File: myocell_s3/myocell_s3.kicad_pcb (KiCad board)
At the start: 4 copper layers, 51 x 68 mm, 102 parts, among them J1 Conn_01x08, J2 IN3P, J3 IN3N, J4 IN4P, J5 Battery Connector JC2, J6 IN4N, J7 USB_C_Receptacle_USB2.0_16P, J8 RLD, Q3 DMG3404L, SW1 SW_Push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

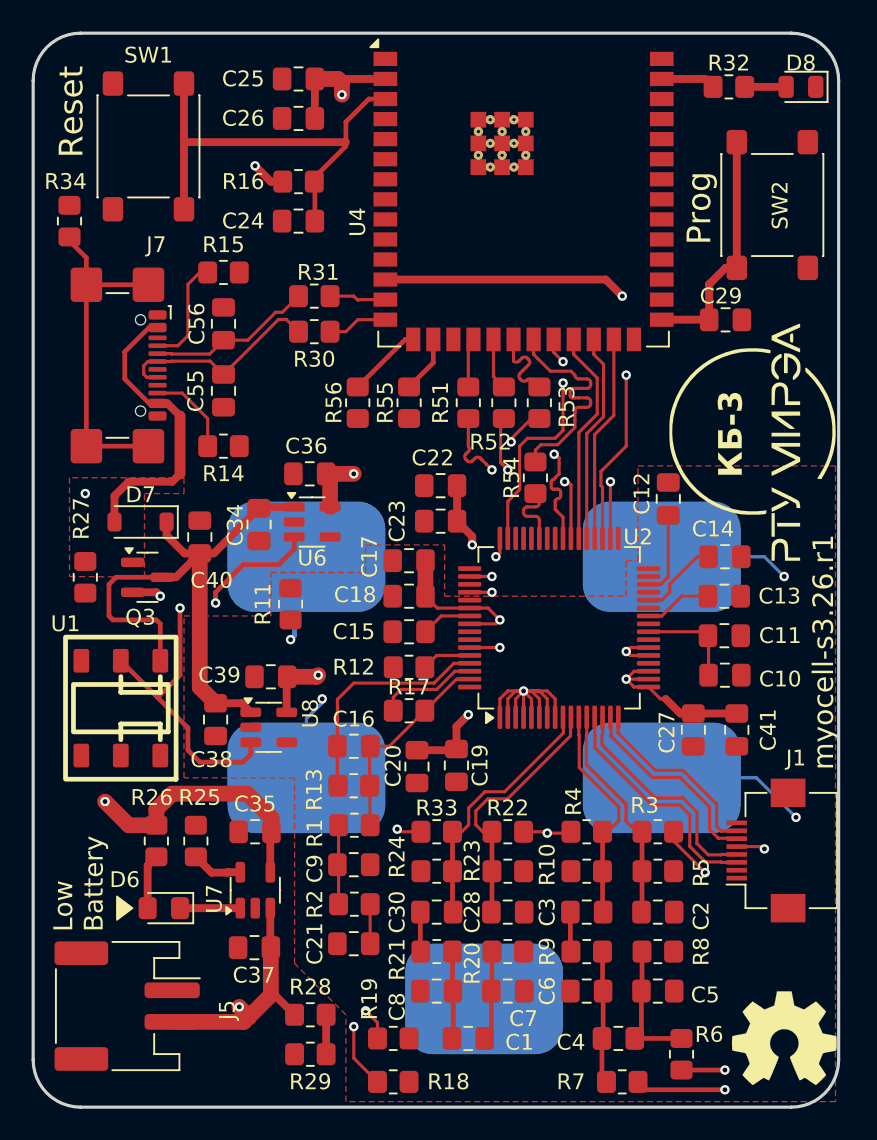
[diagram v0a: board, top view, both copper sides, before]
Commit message: placing polygons
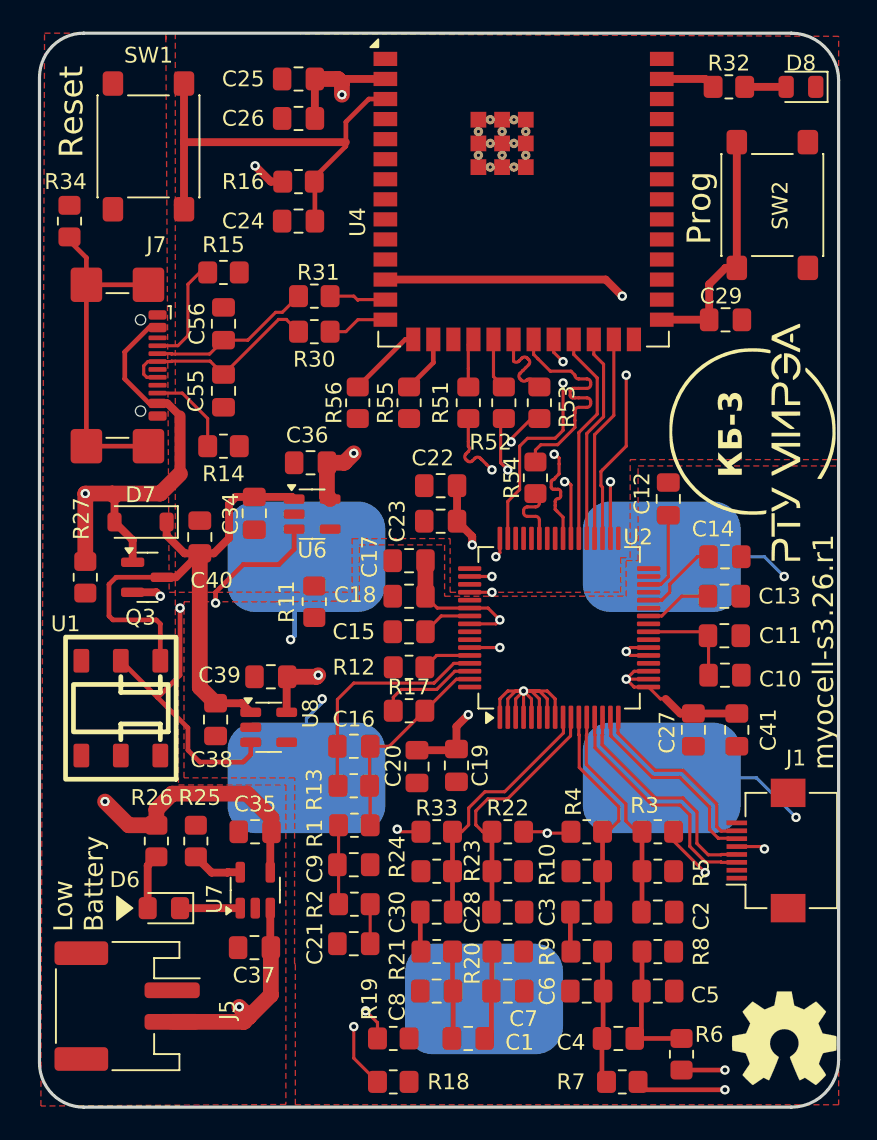
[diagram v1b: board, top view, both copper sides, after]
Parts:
- removed R28, R29: 10k, Resistor_SMD:R_0805_2012Metric_Pad1.20x1.40mm_HandSolder
- moved R11 1.51 mm to (171.0, 85.6)
- moved C34 0.77 mm to (167.2, 80.0)
- moved C36 0.70 mm to (170.8, 76.8)
- moved U6 0.50 mm to (170.9, 80.0)
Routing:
- net /power_supply/VUSB/2.1A: track 55.6 -> 65.0 mm
- net /cpu_wroom_esp32/bat_mon: track 2.50 -> 0.00 mm
- net /power_supply/BAT: track 20.2 -> 18.5 mm
- net VIN: track 37.3 -> 38.9 mm
- net PWR_ENA: track 28.9 -> 29.4 mm
- added copper zone on F.Cu, net GND
- removed copper zone on F.Cu, net /power_supply/VUSB/2.1A
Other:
- board size 51 x 68 mm -> 50.6 x 68 mm

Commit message: polygon tuning
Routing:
- net /adc_8/RLD: track 2.50 -> 34.6 mm, vias 0 -> 2
- net Net-(C1-Pad1): track 5.69 -> 12.2 mm
- net Net-(C1-Pad2): track 5.55 -> 8.26 mm
- net Net-(C28-Pad1): track 0.00 -> 2.52 mm
- net GND: track 0.00 -> 2.45 mm
- added copper zone on B.Cu, net GND
- added copper zone on In1.Cu, net GND
- added copper zone on In1.Cu, net GNDA
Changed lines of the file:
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@@
 		(tags "resistor handsolder")
 		(property "Reference" "R19"
-			(at -1.5 -2.5 90)
+			(at -2.6 -0.05 90)
 			(layer "F.SilkS")
 			(effects
@@
 		(tags "resistor handsolder")
 		(property "Reference" "R14"
-			(at 0 -1.75 180)
+			(at -3.35 1.15 180)
 			(layer "F.SilkS")
 			(effects
@@
 		(tags "capacitor handsolder")
 		(property "Reference" "C8"
-			(at -2.5 1 90)
+			(at -2.75 0.35 180)
 			(layer "F.SilkS")
 			(effects
@@
 		(tags "resistor handsolder")
 		(property "Reference" "R4"
-			(at -0.8375 -1.9125 90)
+			(at 0.15 -1.7625 180)
 			(layer "F.SilkS")
 			(effects
@@
 		(tags "resistor handsolder")
 		(property "Reference" "R8"
-			(at 2.75 0 90)
+			(at 2.75 0 180)
 			(layer "F.SilkS")
 			(effects
@@
 		(tags "connector JST PH horizontal")
 		(property "Reference" "J5"
-			(at 0.25 -6.35 90)
+			(at 3.8 -5.65 180)
 			(layer "F.SilkS")
 			(effects
@@
 		(tags "capacitor handsolder")
 		(property "Reference" "C7"
-			(at 1 1.75 180)
+			(at 0.15 1.55 180)
 			(layer "F.SilkS")
 			(effects
@@
 		(tags "resistor handsolder")
 		(property "Reference" "R5"
-			(at -2.75 -0.0875 90)
+			(at -2.75 -0.0875 180)
 			(layer "F.SilkS")
 			(effects
@@
 		(tags "capacitor handsolder")
 		(property "Reference" "C36"
-			(at -0.2125 -1.75 0)
+			(at 3.6375 0 0)
 			(layer "F.SilkS")
 			(effects
@@
 		(tags "capacitor handsolder")
 		(property "Reference" "C2"
-			(at -2.75 -0.25 90)
+			(at -2.75 -0.25 180)
 			(layer "F.SilkS")
 			(effects
@@
 		(tags "capacitor handsolder")
 		(property "Reference" "C1"
-			(at -3.25 -0.25 0)
+			(at 0.15 1.45 0)
 			(layer "F.SilkS")
 			(effects
@@
 	)
 	(segment
+		(start 196.2 108.8)
+		(end 196.2 103.8)
+		(width 0.2)
+		(layer "F.Cu")
+		(net 11)
+	)
+	(segment
+		(start 174.5375 107.25)
+		(end 174.5375 109.5375)
+		(width 0.2)
+		(layer "F.Cu")
+		(net 11)
+	)
+	(segment
+		(start 196.9 103.1)
+		(end 197.75 103.1)
+		(width 0.2)
+		(layer "F.Cu")
+		(net 11)
+	)
+	(segment
+		(start 174.5375 109.5375)
+		(end 175.2 110.2)
+		(width 0.2)
+		(layer "F.Cu")
+		(net 11)
+	)
+	(segment
+		(start 195.6 109.4)
+		(end 196.2 108.8)
+		(width 0.2)
+		(layer "F.Cu")
+		(net 11)
+	)
+	(segment
+		(start 196.2 103.8)
+		(end 196.9 103.1)
+		(width 0.2)
+		(layer "F.Cu")
+		(net 11)
+	)
+	(via
+		(at 175.2 110.2)
+		(size 0.6)
+		(drill 0.3)
+		(layers "F.Cu" "B.Cu")
+		(net 11)
+	)
+	(via
+		(at 195.6 109.4)
+		(size 0.6)
+		(drill 0.3)
+		(layers "F.Cu" "B.Cu")
+		(net 11)
+	)
+	(segment
+		(start 194.25 110.75)
+		(end 195.6 109.4)
+		(width 0.2)
+		(layer "B.Cu")
+		(net 11)
+	)
+	(segment
+		(start 175.75 110.75)
+		(end 181.75 110.75)
+		(width 0.2)
+		(layer "B.Cu")
+		(net 11)
+	)
+	(segment
+		(start 181.75 110.75)
+		(end 194.25 110.75)
+		(width 0.2)
+		(layer "B.Cu")
+		(net 11)
+	)
+	(segment
+		(start 175.2 110.2)
+		(end 175.75 110.75)
+		(width 0.2)
+		(layer "B.Cu")
+		(net 11)
+	)
+	(segment
 		(start 171.8 76.8)
 		(end 171.8 78.9)
@@
 	)
 	(segment
+		(start 165.3 93.55)
+		(end 164.75 94.1)
+		(width 0.5)
+		(layer "F.Cu")
+		(net 13)
+	)
+	(segment
+		(start 166.975 93.55)
+		(end 165.3 93.55)
+		(width 0.5)
+		(layer "F.Cu")
+		(net 13)
+	)
+	(segment
 		(start 162.75 56.5)
 		(end 162.75 60.75)
@@
 	)
 	(segment
+		(start 179.7125 113.25)
+		(end 177 113.25)
+		(width 0.2)
+		(layer "F.Cu")
+		(net 19)
+	)
+	(segment
 		(start 179.7875 113.175)
 		(end 179.7125 113.25)
@@
 	)
 	(segment
+		(start 181.7875 113.25)
+		(end 181.7875 114.2125)
+		(width 0.2)
+		(layer "F.Cu")
+		(net 20)
+	)
+	(segment
+		(start 181.7875 114.2125)
+		(end 180 116)
+		(width 0.2)
+		(layer "F.Cu")
+		(net 20)
+	)
+	(segment
 		(start 182.2125 110.25)
 		(end 182.2125 112.825)
@@
 	)
 	(segment
+		(start 180 116)
+		(end 177 116)
+		(width 0.2)
+		(layer "F.Cu")
+		(net 20)
+	)
+	(segment
 		(start 187.2125 105.25)
 		(end 187.2125 107.7125)
@@
 	)
 	(segment
+		(start 184.2875 105.25)
+		(end 184.2875 107.7125)
+		(width 0.2)
+		(layer "F.Cu")
+		(net 31)
+	)
+	(segment
+		(start 184.2875 107.7125)
+		(end 184.25 107.75)
+		(width 0.2)
+		(layer "F.Cu")
+		(net 31)
+	)
+	(segment
 		(start 177.7125 107.7125)
 		(end 177.75 107.75)
@@
 		(net 1)
 		(net_name "GNDA")
-		(layer "F.Cu")
+		(layers "F.Cu" "In1.Cu")
 		(hatch edge 0.5)
 		(priority 8)
@@
 			(thermal_gap 0.5)
 			(thermal_bridge_width 0.5)
+			(island_removal_mode 1)
+			(island_area_min 10)
 		)
 		(polygon
 			(pts
 				(xy 173.85 82) (xy 179.25 82) (xy 179.25 85.25) (xy 190.75 85.25) (xy 190.75 83) (xy 191.5 83) (xy 191.5 77)
-				(xy 204.2 77) (xy 204.2 117.45) (xy 169.8 117.45) (xy 169.8 108.55) (xy 169.75 108.5) (xy 169.75 96.75)
-				(xy 162.75 96.75) (xy 162.75 85.6) (xy 168.4 85.6) (xy 168.4 85.6) (xy 173.85 85.554583)
+				(xy 204.2 77) (xy 204.2 117.65) (xy 169.8 117.65) (xy 169.8 96.95) (xy 162.549103 96.95) (xy 162.599996 85.600822)
+				(xy 173.85 85.554583)
 			)
 		)
@@
 		(net 13)
 		(net_name "GND")
-		(layer "F.Cu")
+		(layers "F.Cu" "In1.Cu")
 		(hatch edge 0.5)
 		(connect_pads
@@
 			(thermal_gap 0.5)
 			(thermal_bridge_width 0.5)
+			(island_removal_mode 1)
+			(island_area_min 10)
 		)
 		(polygon
 			(pts
-				(xy 161.6 49.8) (xy 161.810779 85) (xy 173.4 85) (xy 173.4 81.6) (xy 179.6 81.6) (xy 179.6 85) (xy 190.4 85)
-				(xy 190.4 82.8) (xy 191 82.8) (xy 191 76.6) (xy 204.2 76.6) (xy 204.2 49.8) (xy 161.6 49.6) (xy 161.6 50)
+				(xy 160.8 49.594312) (xy 160.8 85) (xy 173.4 85) (xy 173.4 81.6) (xy 179.6 81.6) (xy 179.6 84.8)
+				(xy 190.2 84.8) (xy 190.2 82.6) (xy 191 82.6) (xy 191 76.6) (xy 204.2 76.6) (xy 204.2 49.8)
 			)
 		)
@@
 		(net 13)
 		(net_name "GND")
-		(layer "F.Cu")
+		(layers "F.Cu" "In1.Cu")
 		(hatch edge 0.5)
 		(priority 9)
@@
 		(polygon
 			(pts
-				(xy 153.920224 49.6) (xy 162.2 49.6) (xy 162.2 90.6) (xy 162.4 90.6) (xy 162.4 97.2) (xy 169.2 97.2)
-				(xy 169.2 117.430216) (xy 153.68953 117.527844)
+				(xy 153.582646 49.6) (xy 161.982646 49.6) (xy 161.982646 97.6) (xy 169.382646 97.6) (xy 169.382646 117.6)
+				(xy 153.582646 117.6)
+			)
+		)
+	)
+	(zone
+		(net 13)
+		(net_name "GND")
+		(layer "B.Cu")
+		(hatch edge 0.5)
+		(connect_pads
+			(clearance 0.2)
+		)
+		(min_thickness 0.2)
+		(filled_areas_thickness no)
+		(fill yes
+			(thermal_gap 0.5)
+			(thermal_bridge_width 0.5)
+			(island_removal_mode 1)
+			(island_area_min 10)
+		)
+		(polygon
+			(pts
+				(xy 153.6 49.6) (xy 204.2 49.6) (xy 204.2 117.6) (xy 153.6 117.6)
 			)
 		)

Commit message: start DRC
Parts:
- moved REF** 0.86 mm to (200.6, 112.4)
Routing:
- net /usb_d-: track 10.5 -> 15.8 mm, vias 0 -> 2
- net Net-(C2-Pad1): track 0.00 -> 2.52 mm
- net +3.3V: track 62.7 -> 65.0 mm, vias 7 -> 6
- net PWR_ENA: track 29.4 -> 27.1 mm
- net GND: track 2.45 -> 1.56 mm, vias 0 -> 3

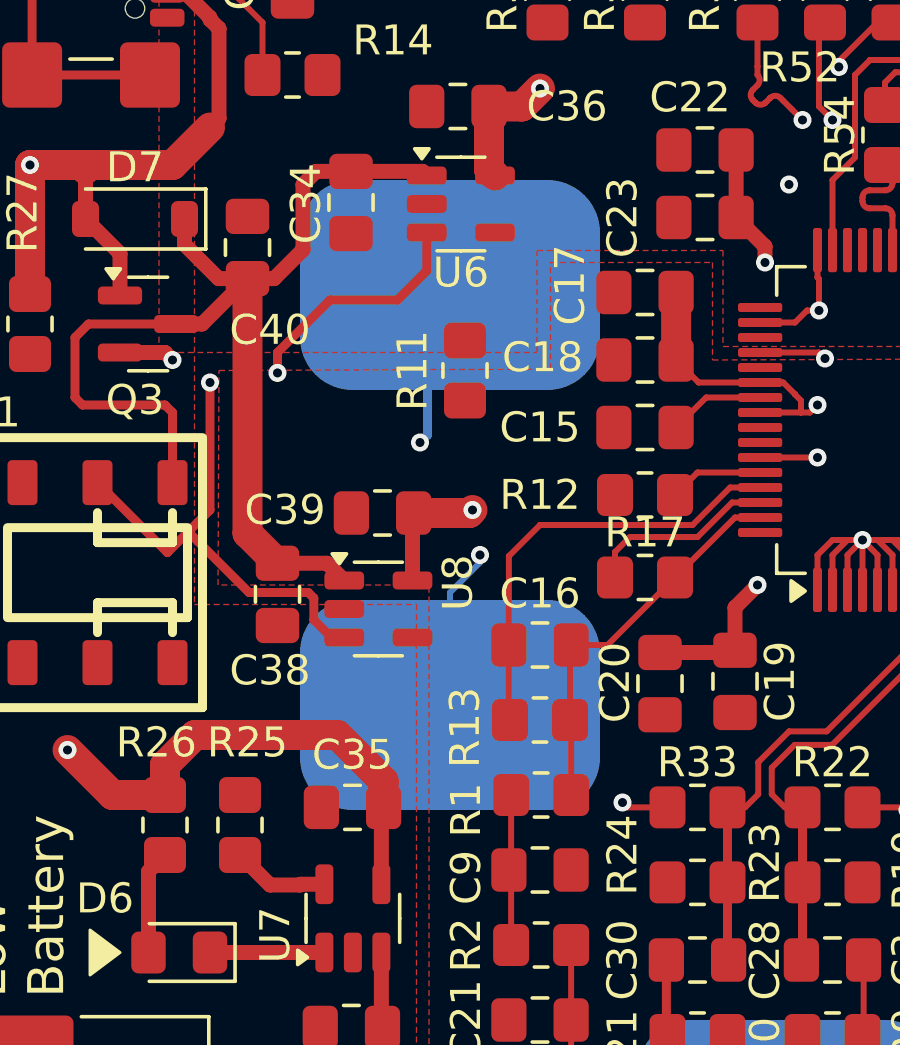
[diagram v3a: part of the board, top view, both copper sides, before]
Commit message: adjust electrode positions
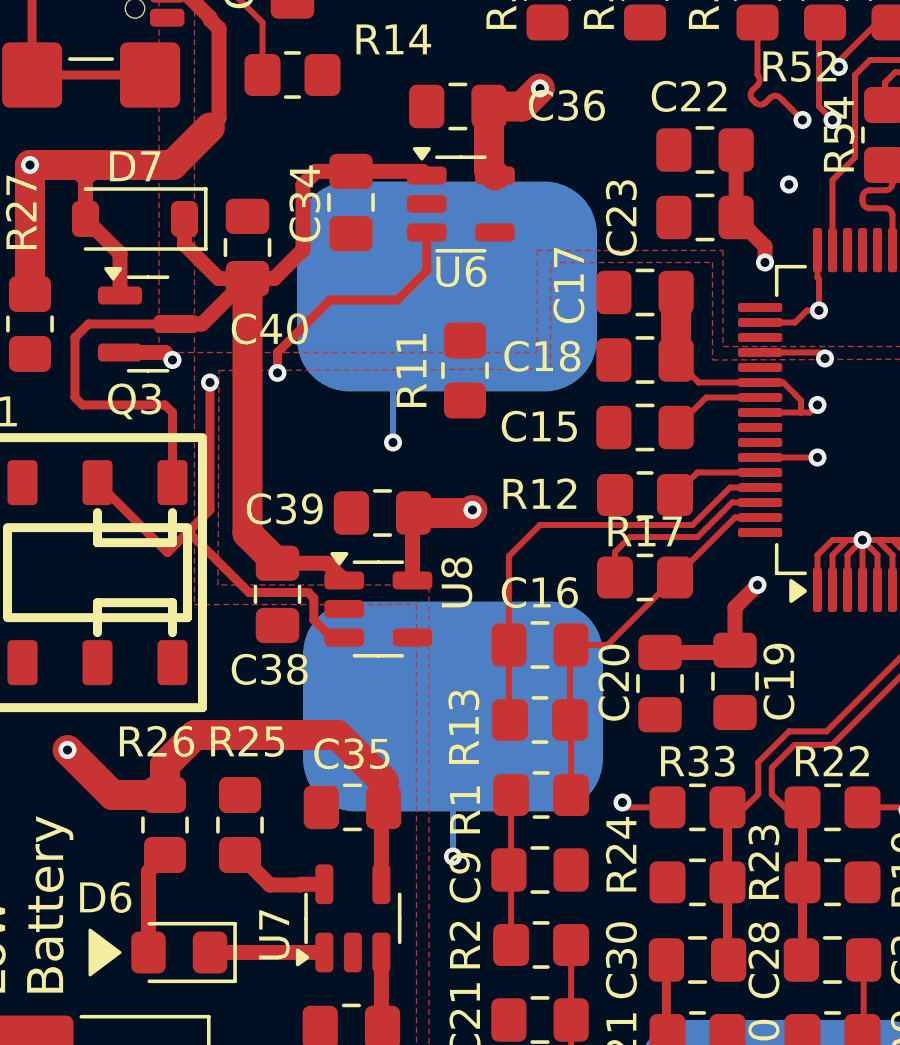
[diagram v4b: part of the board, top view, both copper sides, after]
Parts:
- moved J4 14.1 mm to (170.6, 96.8)
- moved J6 14.0 mm to (170.4, 82.8)
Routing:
- net /adc_8/in4f+: track 35.4 -> 21.0 mm
- net /adc_8/in4f-: track 28.9 -> 34.1 mm
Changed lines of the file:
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@@
 	(footprint "emg:EMG_PAD_10_7"
 		(layer "B.Cu")
-		(at 170.5 82.75 180)
+		(at 170.6 96.8 180)
 		(property "Reference" "J4"
 			(at -6.25 6 0)
@@
 	(footprint "emg:EMG_PAD_10_7"
 		(layer "B.Cu")
-		(at 170.5 96.75 180)
+		(at 170.4 82.8 180)
 		(property "Reference" "J6"
 			(at -6.75 6 0)
@@
 		)
 	)
+	(dimension
+		(type orthogonal)
+		(layer "Dwgs.User")
+		(pts
+			(xy 204.2 117.65) (xy 204.2 49.8)
+		)
+		(height 5.6)
+		(orientation 1)
+		(format
+			(prefix "")
+			(suffix "")
+			(units 3)
+			(units_format 1)
+			(precision 4)
+		)
+		(style
+			(thickness 0.1)
+			(arrow_length 1.27)
+			(text_position_mode 0)
+			(arrow_direction outward)
+			(extension_height 0.58642)
+			(extension_offset 0.5)
+			(keep_text_aligned yes)
+		)
+		(gr_text "67.8500 mm"
+			(at 208.65 83.725 90)
+			(layer "Dwgs.User")
+			(effects
+				(font
+					(size 1 1)
+					(thickness 0.15)
+				)
+			)
+		)
+	)
+	(dimension
+		(type orthogonal)
+		(layer "Dwgs.User")
+		(pts
+			(xy 153.6 117.6) (xy 204.2 117.6)
+		)
+		(height 6.2)
+		(orientation 0)
+		(format
+			(prefix "")
+			(suffix "")
+			(units 3)
+			(units_format 1)
+			(precision 4)
+		)
+		(style
+			(thickness 0.1)
+			(arrow_length 1.27)
+			(text_position_mode 0)
+			(arrow_direction outward)
+			(extension_height 0.58642)
+			(extension_offset 0.5)
+			(keep_text_aligned yes)
+		)
+		(gr_text "50.6000 mm"
+			(at 178.9 122.65 0)
+			(layer "Dwgs.User")
+			(effects
+				(font
+					(size 1 1)
+					(thickness 0.15)
+				)
+			)
+		)
+	)
 	(segment
 		(start 172.4625 102.7125)
@@
 	)
 	(via
-		(at 169.5 88)
+		(at 170.6 101.8)
 		(size 0.6)
 		(drill 0.3)
@@
 	)
 	(segment
-		(start 169.75 83)
-		(end 169.75 87.75)
-		(width 0.3)
-		(layer "B.Cu")
-		(net 93)
-	)
-	(segment
-		(start 169.75 87.75)
-		(end 169.5 88)
-		(width 0.3)
-		(layer "B.Cu")
-		(net 93)
-	)
-	(segment
-		(start 169.5 90.725)
-		(end 169.5 88)
+		(start 170.6 101.8)
+		(end 170.6 96.8)
 		(width 0.2)
-		(layer "In2.Cu")
+		(layer "B.Cu")
 		(net 93)
 	)
 	(segment
-		(start 170.775 92)
-		(end 169.5 90.725)
+		(start 170.775 109.093199)
+		(end 170.775 101.975)
 		(width 0.2)
 		(layer "In2.Cu")
@@
 	)
 	(segment
-		(start 173.5 111.818199)
-		(end 170.775 109.093199)
+		(start 173.5 112.5)
+		(end 173.5 111.818199)
 		(width 0.2)
 		(layer "In2.Cu")
@@
 	)
 	(segment
-		(start 170.775 109.093199)
-		(end 170.775 92)
+		(start 170.775 101.975)
+		(end 170.6 101.8)
 		(width 0.2)
 		(layer "In2.Cu")
@@
 	)
 	(segment
-		(start 173.5 112.5)
-		(end 173.5 111.818199)
+		(start 173.5 111.818199)
+		(end 170.775 109.093199)
 		(width 0.2)
 		(layer "In2.Cu")
@@
 	)
 	(via
-		(at 171.5 91.75)
+		(at 168.6 88)
 		(size 0.6)
 		(drill 0.3)
@@
 	)
 	(segment
-		(start 171.5 91.75)
-		(end 171.5 92)
+		(start 168.6 88)
+		(end 168.6 84.6)
 		(width 0.2)
 		(layer "B.Cu")
@@
 	)
 	(segment
-		(start 171.5 92)
-		(end 170.5 93)
+		(start 168.6 84.6)
+		(end 170.4 82.8)
 		(width 0.2)
 		(layer "B.Cu")
@@
 	)
 	(segment
-		(start 170.5 93)
-		(end 170.5 96.75)
+		(start 168.6 90.681802)
+		(end 168.6 88)
 		(width 0.2)
-		(layer "B.Cu")
+		(layer "In2.Cu")
 		(net 94)
 	)
 	(segment
-		(start 171.225 92)
-		(end 171.25 92)
+		(start 171.225 108.906801)
+		(end 171.225 93.306802)
 		(width 0.2)
 		(layer "In2.Cu")
@@
 	)
 	(segment
-		(start 171.25 92)
-		(end 171.5 91.75)
+		(start 171.225 93.306802)
+		(end 168.759099 90.840901)
 		(width 0.2)
 		(layer "In2.Cu")
@@
 	)
 	(segment
-		(start 171.225 108.906801)
-		(end 171.225 92)
+		(start 168.759099 90.840901)
+		(end 168.6 90.681802)
 		(width 0.2)
 		(layer "In2.Cu")
@@
 			(pts
 				(xy 160.8 49.594312) (xy 160.8 85) (xy 173.4 85) (xy 173.4 81.6) (xy 179.6 81.6) (xy 179.6 84.8)
-				(xy 191 84.8) (xy 191 82.6) (xy 191 82.6) (xy 191 76.6) (xy 204.2 76.6) (xy 204.2 49.8)
+				(xy 191 84.8) (xy 191 82.6) (xy 191 76.6) (xy 204.2 76.6) (xy 204.2 49.8)
 			)
 		)

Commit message: DRC
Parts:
- added R28: 10k, Resistor_SMD:R_0805_2012Metric_Pad1.20x1.40mm_HandSolder, F.Cu at (156.2, 84.8)
- added R29: 10k, Resistor_SMD:R_0805_2012Metric_Pad1.20x1.40mm_HandSolder, F.Cu at (170.0, 63.6)
- moved R27 3.86 mm to (156.2, 80.2)
- moved R30 1.35 mm to (170.0, 69.4)
- moved R31 1.25 mm to (170.0, 67.0)
- moved R16 0.80 mm to (170.0, 58.2)
- moved C24 0.70 mm to (170.0, 60.8)
- moved R14 0.29 mm to (165.4, 76.0)
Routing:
- net /cpu_wroom_esp32/bat_mon: track 0.00 -> 45.5 mm, vias 0 -> 2
- net VIN: track 38.9 -> 32.3 mm
- net /power_supply/BAT: track 18.5 -> 22.1 mm
- net PWR_ENA: track 27.1 -> 30.6 mm
- net /power_supply/VUSB/2.1A: track 65.2 -> 62.3 mm
- net GND: track 1.56 -> 4.02 mm, vias 3 -> 11
- net /usb_d+: track 13.5 -> 11.5 mm
- net /cpu_wroom_esp32/D-: track 3.62 -> 5.53 mm
- net /cpu_wroom_esp32/D+: track 3.81 -> 5.53 mm
- net /adc_8/in4f-: track 34.1 -> 34.8 mm
- net GNDA: vias 0 -> 1

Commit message: sent to rezonit
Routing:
- net GNDA: vias 1 -> 26
- net GND: vias 11 -> 32
